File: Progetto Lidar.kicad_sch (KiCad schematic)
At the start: 33 parts, among them IC1 TLV74133PDBVR, IC2 LT1719IS6#TRPBF, J1 CONN_LASER, J10 Conn_01x08, J2 CONN_RICEVITORE, J3 Conn_02x18_Odd_Even, J4 Conn_01x10, J5 Conn_01x08, J6 Conn_01x08, J7 Conn_01x08, J8 Conn_SPI, J9 Conn_01x08, Y1 SiT2024BA-S2-33E-8.000000G

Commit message: Aggiunto pinou di Arduino su silkscreen
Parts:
- D1: value 5V_LED -> 5V
- D2: value 3V3_LED -> 3V3
- renumbered A1 to IC_0, Y1 to IC_2, IC_2 to IC_3, IC2 to IC_4, IC1 to IC_5
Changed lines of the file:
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@@
   )
   (text "-5V) (5-1.8)/0.002= 1600 -> 1k8\n\n-3V3)  (3.3-1.8)/0.002=750 -> 820"
-    (at 255.905 262.89 0)
+    (at 255.905 263.525 0)
     (effects (font (size 1.27 1.27)) (justify left bottom))
   )
@@
   (symbol (lib_id "Libreria_componenti:LT1719IS6#TRPBF") (at 321.31 175.26 0) (unit 1)
     (in_bom yes) (on_board yes)
-    (property "Reference" "IC2" (id 0) (at 335.28 168.275 0))
+    (property "Reference" "IC_4" (id 0) (at 335.28 168.275 0))
     (property "Value" "LT1719IS6#TRPBF" (id 1) (at 335.28 170.815 0))
     (property "Footprint" "Libreria_componenti_footprint:SOT95P280X100-6N" (id 2) (at 321.31 175.26 0)
@@
   )
   (symbol (lib_id "arduino-library:Arduino_Due_Shield") (at 128.27 88.9 180) (unit 1)
-    (in_bom yes) (on_board yes) (fields_autoplaced)
-    (property "Reference" "A1" (id 0) (at 128.27 152.4 0)
+    (in_bom yes) (on_board yes)
+    (property "Reference" "IC_0" (id 0) (at 128.27 88.9 0)
       (effects (font (size 1.524 1.524)))
     )
-    (property "Value" "Arduino_Due_Shield" (id 1) (at 128.27 148.59 0)
+    (property "Value" "Arduino_Due_Shield" (id 1) (at 128.27 94.615 0)
       (effects (font (size 1.524 1.524)))
     )
@@
       (effects (font (size 1.27 1.27)) (justify right))
     )
-    (property "Value" "5V_LED" (id 1) (at 292.735 240.665 90)
+    (property "Value" "5V" (id 1) (at 292.735 240.665 90)
       (effects (font (size 1.27 1.27)) (justify right))
     )
@@
   (symbol (lib_id "Libreria_componenti:TLV74133PDBVR") (at 317.5 229.235 0) (unit 1)
     (in_bom yes) (on_board yes)
-    (property "Reference" "IC1" (id 0) (at 330.2 220.98 0))
+    (property "Reference" "IC_5" (id 0) (at 330.2 220.98 0))
     (property "Value" "TLV74133PDBVR" (id 1) (at 330.2 223.52 0))
     (property "Footprint" "Libreria_componenti_footprint:SOT95P280X145-5N" (id 2) (at 327.66 239.395 0)
@@
       (effects (font (size 1.27 1.27)) (justify right))
     )
-    (property "Value" "3V3_LED" (id 1) (at 377.19 239.7124 90)
+    (property "Value" "3V3" (id 1) (at 377.19 239.7124 90)
       (effects (font (size 1.27 1.27)) (justify right))
     )
@@
   (symbol (lib_id "Libreria_componenti:SiT2024BA-S2-33E-8.000000G") (at 316.865 81.915 0) (unit 1)
     (in_bom yes) (on_board yes)
-    (property "Reference" "Y1" (id 0) (at 330.835 74.295 0))
+    (property "Reference" "IC_2" (id 0) (at 330.835 74.295 0))
     (property "Value" "SiT2024BA-S2-33E-8.000000G" (id 1) (at 330.835 76.835 0))
     (property "Footprint" "Libreria_componenti_footprint:SOT95P280X145-5N" (id 2) (at 316.865 81.915 0)
@@
   (symbol (lib_id "Libreria_componenti:SN74LVC1G125DCKR") (at 304.165 128.27 0) (unit 1)
     (in_bom yes) (on_board yes)
-    (property "Reference" "IC_2" (id 0) (at 316.865 121.285 0))
+    (property "Reference" "IC_3" (id 0) (at 316.865 121.285 0))
     (property "Value" "SN74LVC1G125DCKR" (id 1) (at 316.865 123.825 0))
     (property "Footprint" "Libreria_componenti_footprint:SOT65P210X110-5N" (id 2) (at 304.165 128.27 0)
@@
       (reference "#PWR0122") (unit 1) (value "GND") (footprint "")
     )
-    (path "/2e4e510e-4a1a-4b96-8e55-c9f0bcdfd785"
-      (reference "A1") (unit 1) (value "Arduino_Due_Shield") (footprint "arduino-library:Arduino_Due_Shield")
-    )
     (path "/43c97b09-60c8-4d38-9787-f7da828e3980"
       (reference "C1") (unit 1) (value "0.1uF") (footprint "Capacitor_SMD:C_0805_2012Metric")
@@
     )
     (path "/41b8cd4c-a10e-4a5f-882d-d8e02fdcfc5a"
-      (reference "D1") (unit 1) (value "5V_LED") (footprint "LED_SMD:LED_0805_2012Metric")
+      (reference "D1") (unit 1) (value "5V") (footprint "LED_SMD:LED_0805_2012Metric")
     )
     (path "/935bfb98-00d0-4874-b27c-8afbf508f578"
-      (reference "D2") (unit 1) (value "3V3_LED") (footprint "LED_SMD:LED_0805_2012Metric")
-    )
-    (path "/80c739b2-bfd7-4196-b999-8fa7f79fdf43"
-      (reference "IC1") (unit 1) (value "TLV74133PDBVR") (footprint "Libreria_componenti_footprint:SOT95P280X145-5N")
-    )
-    (path "/1f41963f-b620-49ed-9e39-222e710c0a60"
-      (reference "IC2") (unit 1) (value "LT1719IS6#TRPBF") (footprint "Libreria_componenti_footprint:SOT95P280X100-6N")
+      (reference "D2") (unit 1) (value "3V3") (footprint "LED_SMD:LED_0805_2012Metric")
+    )
+    (path "/2e4e510e-4a1a-4b96-8e55-c9f0bcdfd785"
+      (reference "IC_0") (unit 1) (value "Arduino_Due_Shield") (footprint "arduino-library:Arduino_Due_Shield")
     )
     (path "/48194ae1-f8df-4010-bbe3-4a700fb0cf99"
       (reference "IC_1") (unit 1) (value "TDC7200PW") (footprint "Libreria_componenti_footprint:SOP65P640X120-14N")
     )
+    (path "/c6b204f7-0037-47cd-baa9-5dbf5fe1ca64"
+      (reference "IC_2") (unit 1) (value "SiT2024BA-S2-33E-8.000000G") (footprint "Libreria_componenti_footprint:SOT95P280X145-5N")
+    )
     (path "/e6367b0f-ad1b-4084-86e1-5df88bd77834"
-      (reference "IC_2") (unit 1) (value "SN74LVC1G125DCKR") (footprint "Libreria_componenti_footprint:SOT65P210X110-5N")
+      (reference "IC_3") (unit 1) (value "SN74LVC1G125DCKR") (footprint "Libreria_componenti_footprint:SOT65P210X110-5N")
+    )
+    (path "/1f41963f-b620-49ed-9e39-222e710c0a60"
+      (reference "IC_4") (unit 1) (value "LT1719IS6#TRPBF") (footprint "Libreria_componenti_footprint:SOT95P280X100-6N")
+    )
+    (path "/80c739b2-bfd7-4196-b999-8fa7f79fdf43"
+      (reference "IC_5") (unit 1) (value "TLV74133PDBVR") (footprint "Libreria_componenti_footprint:SOT95P280X145-5N")
     )
     (path "/0953ec08-2b6e-49e4-9513-dc10befe5ad7"
@@
       (reference "R3") (unit 1) (value "820") (footprint "Resistor_SMD:R_0805_2012Metric")
     )
-    (path "/c6b204f7-0037-47cd-baa9-5dbf5fe1ca64"
-      (reference "Y1") (unit 1) (value "SiT2024BA-S2-33E-8.000000G") (footprint "Libreria_componenti_footprint:SOT95P280X145-5N")
-    )
-  )
+  )

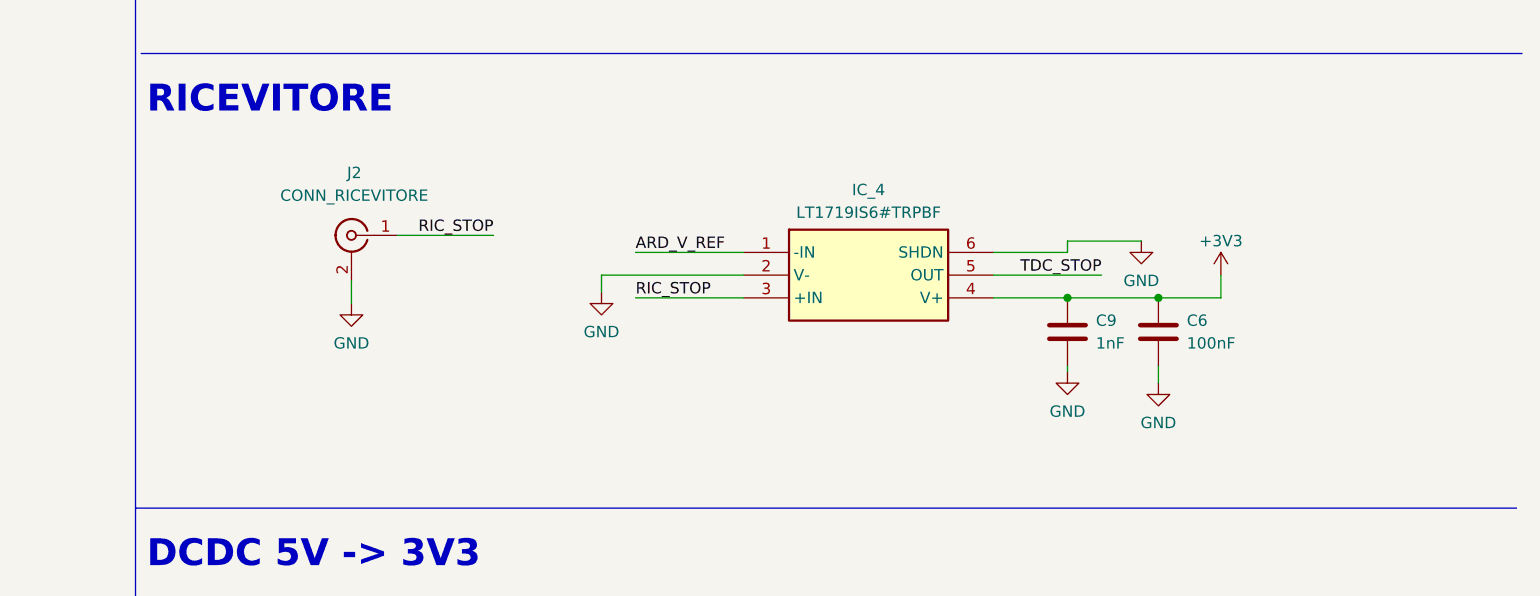
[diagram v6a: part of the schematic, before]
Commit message: Corretto simulazione, aggiunto circuito di condizionamento del segnale e modificato il layout
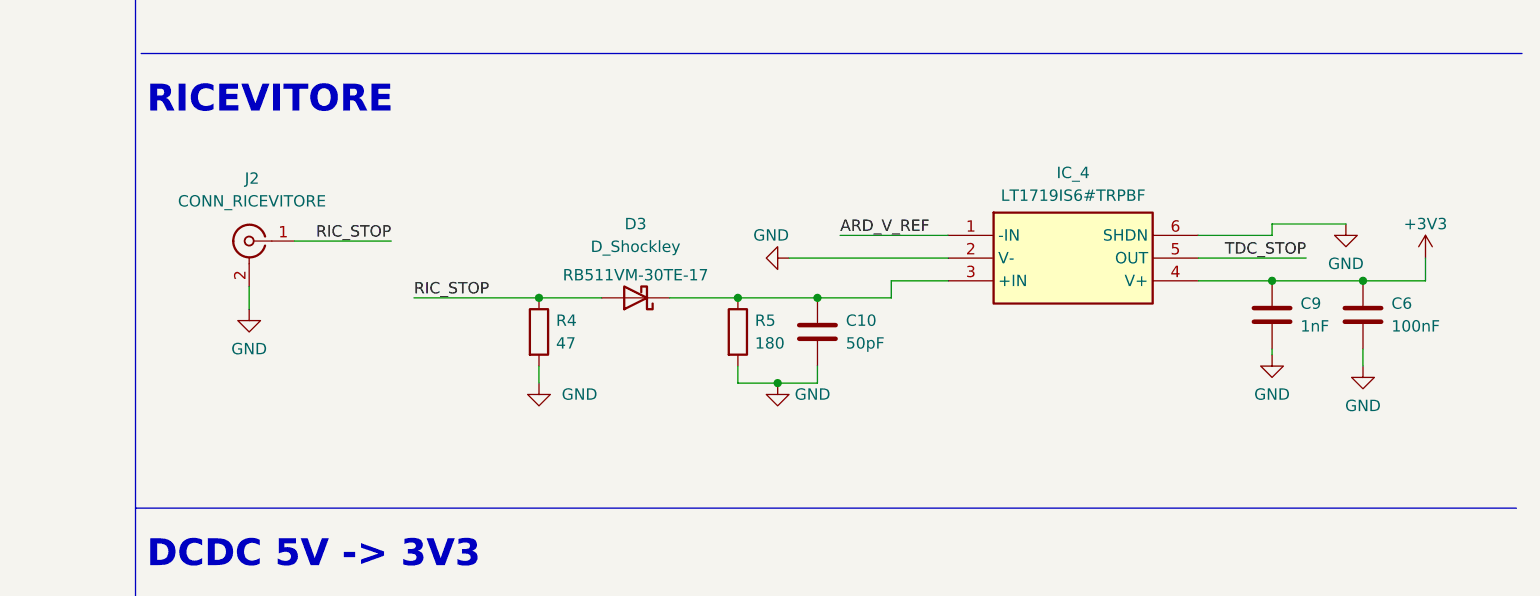
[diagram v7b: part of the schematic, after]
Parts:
- added C10: 50pF, Capacitor_SMD:C_0805_2012Metric, symbol Device:C
- added D3: D_Shockley, Libreria_componenti_footprint:RB511VM30TE17, symbol Device:D_Schottky
- added R4: 47, Resistor_SMD:R_0805_2012Metric, symbol Device:R
- added R5: 180, Resistor_SMD:R_0805_2012Metric, symbol Device:R
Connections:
- net GND: now also C10.2, R4.2, R5.2
- net RIC_STOP: now also D3.2 (A), R4.1; no longer IC_4.3 (+IN)
- new net: C10.1, D3.1 (K), IC_4.3 (+IN), R5.1
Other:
- moved on the sheet: C6, C9, IC_4, J2

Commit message: Sistemato alcuni errori di circuito, aggiunto resistenze per SPI, aggiunto condensatori di filtraggio
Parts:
- added C11, C12: 1nF, Capacitor_SMD:C_0805_2012Metric, symbol Device:C
- added R10, R6, R7, R8, R9: 100, Resistor_SMD:R_0805_2012Metric, symbol Device:R
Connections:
- net +3V3: now also C11.1, C12.1
- net GND: now also C11.2, C12.2, R10.1; no longer IC_4.6 (SHDN)
- net SPI_CS: now also R6.1; no longer IC_0.D44, J3.25 (Pin_25)
- net SPI_MISO: now also R9.1; no longer IC_1.9 (DOUT)
- net SPI_MOSI: now also R7.2; no longer IC_0.MOSI (SPI_MOSI)
- net SPI_SCK: now also R8.2; no longer IC_0.SCK (SPI_SCK)
- new net: IC_4.6 (SHDN), R10.2
- new net: IC_0.MOSI (SPI_MOSI), R7.1
- new net: IC_0.SCK (SPI_SCK), R8.1
- new net: IC_1.9 (DOUT), R9.2
- new net ARD_GPIO_44: IC_0.D44, J3.25 (Pin_25), R6.2
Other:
- moved on the sheet: C3, C4, C7
